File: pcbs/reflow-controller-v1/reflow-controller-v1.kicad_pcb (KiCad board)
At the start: 4 copper layers, 85.2 x 238.5 mm, 137 parts, among them J1 PinHeader 1x03 P2.54mm, J101 EB163A-03-C-180, J102 EB163A-02-C-180, J103 EB163A-02-C-180, J104 EB163A-02-C-180, J105 EB163A-02-C-180, J106 PinHeader 1x03 P2.54mm, J1101 EB163A-04-C-180, J1201 EB163A-04-C-180, J1301 EB163A-04-C-180, J2 PinHeader 1x02 P2.54mm, J3 SWD, J4 UART, M101 47053-1000, Q1 PMV65XP, SW1001 TS04-66-85-BK-160-SMT, SW1002 PEC12R-3220F-S0024, SW1003 TS04-66-85-BK-160-SMT, U1 TMP1075DSG, U1101 MAX31865ATP+, U1201 MAX31865ATP+, U1301 MAX31865ATP+, U2 TMP1075DSG, U201 TPS62933DRLR, U3 STM32G474VETx, U301 MOC3043SM, U401 MOC3043SM, U501 MOC3043SM, U601 MOC3043SM

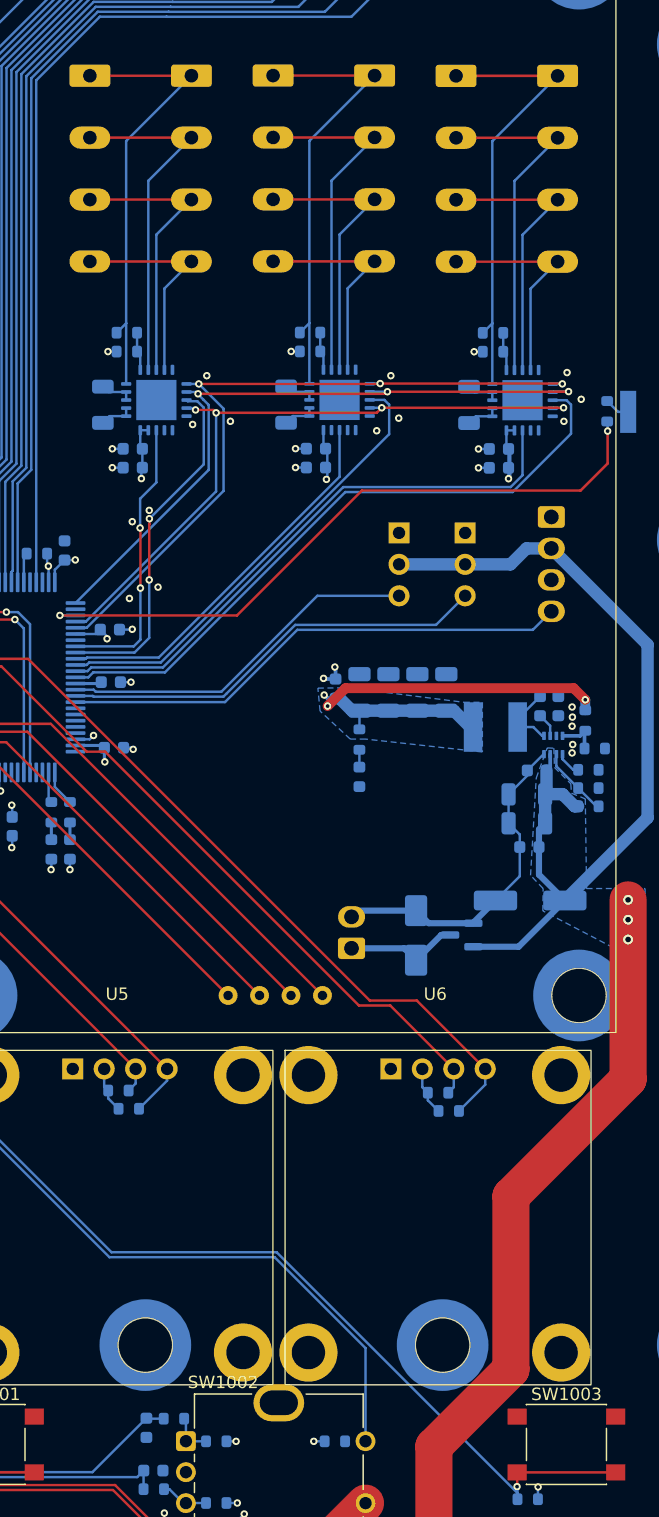
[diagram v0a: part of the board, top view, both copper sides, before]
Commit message: improve dfn qfn fanouts
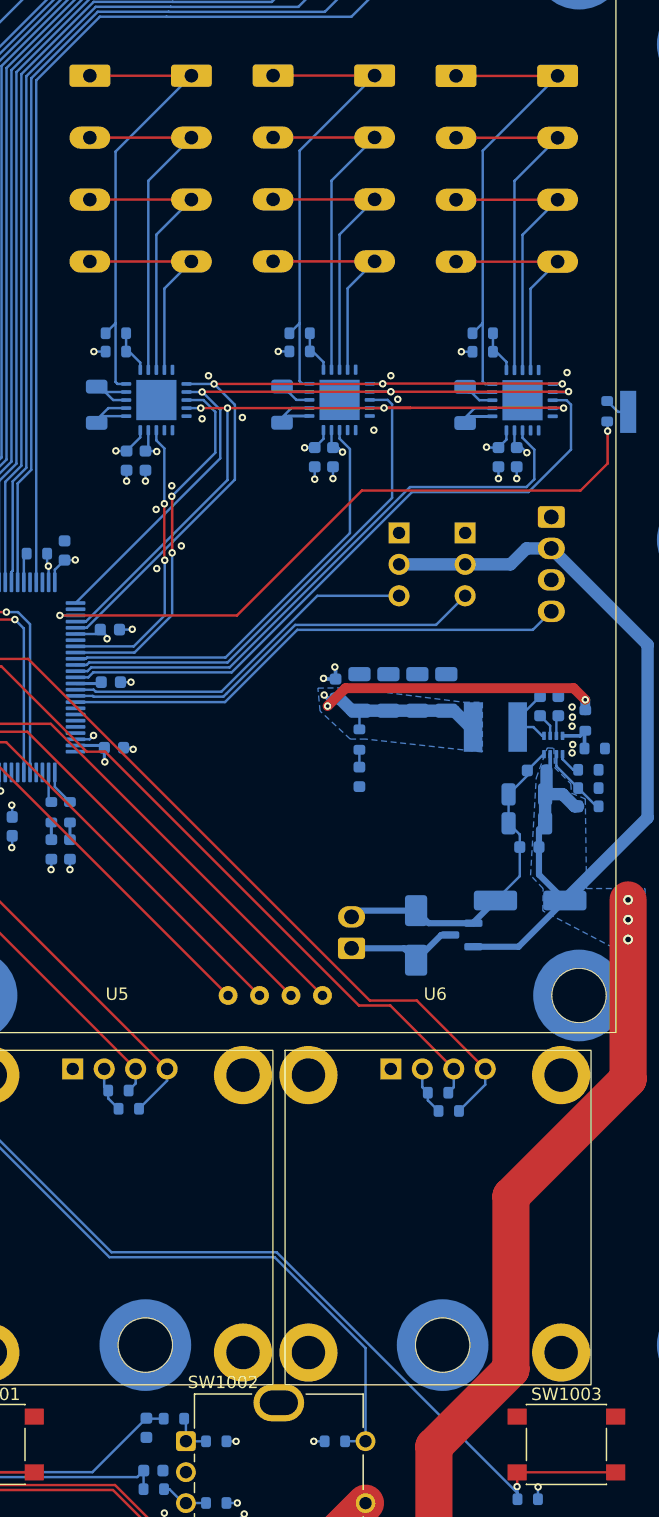
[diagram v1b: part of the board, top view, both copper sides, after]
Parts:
- moved C1302 1.67 mm to (82.5, 59.5), turned to -90 degrees
- moved C1202 1.61 mm to (67.7, 59.5), turned to -90 degrees
- moved C1101 1.17 mm to (52.6, 59.8), turned to -90 degrees
- moved C1102 1.08 mm to (51.1, 59.8), turned to -90 degrees
- moved R1103 0.89 mm to (50.2, 49.5)
- moved R1102 0.88 mm to (50.2, 51.0)
- moved R1203 0.84 mm to (65.0, 49.5)
- moved R1201 0.84 mm to (65.0, 51.0)
- moved R1303 0.83 mm to (79.8, 49.5)
- moved R1301 0.83 mm to (79.8, 51.0)
- moved C1201 0.70 mm to (66.2, 59.5), turned to -90 degrees
- moved C1301 0.66 mm to (81.1, 59.5), turned to -90 degrees
- moved R1101 0.50 mm to (48.6, 55.3)
- moved R1202 0.33 mm to (63.6, 55.3)
- moved R1302 0.32 mm to (78.4, 55.3)
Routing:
- net Net-(U1201-BIAS): track 2.76 -> 8.06 mm
- net Net-(U1301-BIAS): track 2.76 -> 8.05 mm
- net Net-(U1201-ISENSOR): track 2.71 -> 7.77 mm
- net Net-(U1301-ISENSOR): track 2.71 -> 7.76 mm
- net /Temperature sensor 2/~{DRDY}: track 31.2 -> 35.0 mm
- net /Temperature sensor 2/~{CS}: track 37.1 -> 40.7 mm
- net Net-(U1101-BIAS): track 2.76 -> 5.63 mm
- net /Temperature sensor 1/SDO: track 54.7 -> 57.5 mm
- net Net-(U1101-ISENSOR): track 2.71 -> 5.39 mm
- net /AC DC Converter/SS: track 0.00 -> 1.69 mm
- net /Buttons/SW_Encoder: track 79.5 -> 81.2 mm
- net /Temperature sensor 3/~{DRDY}: track 46.3 -> 47.8 mm
- net /Temperature sensor 1/SCLK: track 55.4 -> 56.6 mm
- net /Temperature sensor 1/FORCE+: track 36.4 -> 37.5 mm
- net /Temperature sensor 1/~{CS}: track 28.5 -> 29.6 mm
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
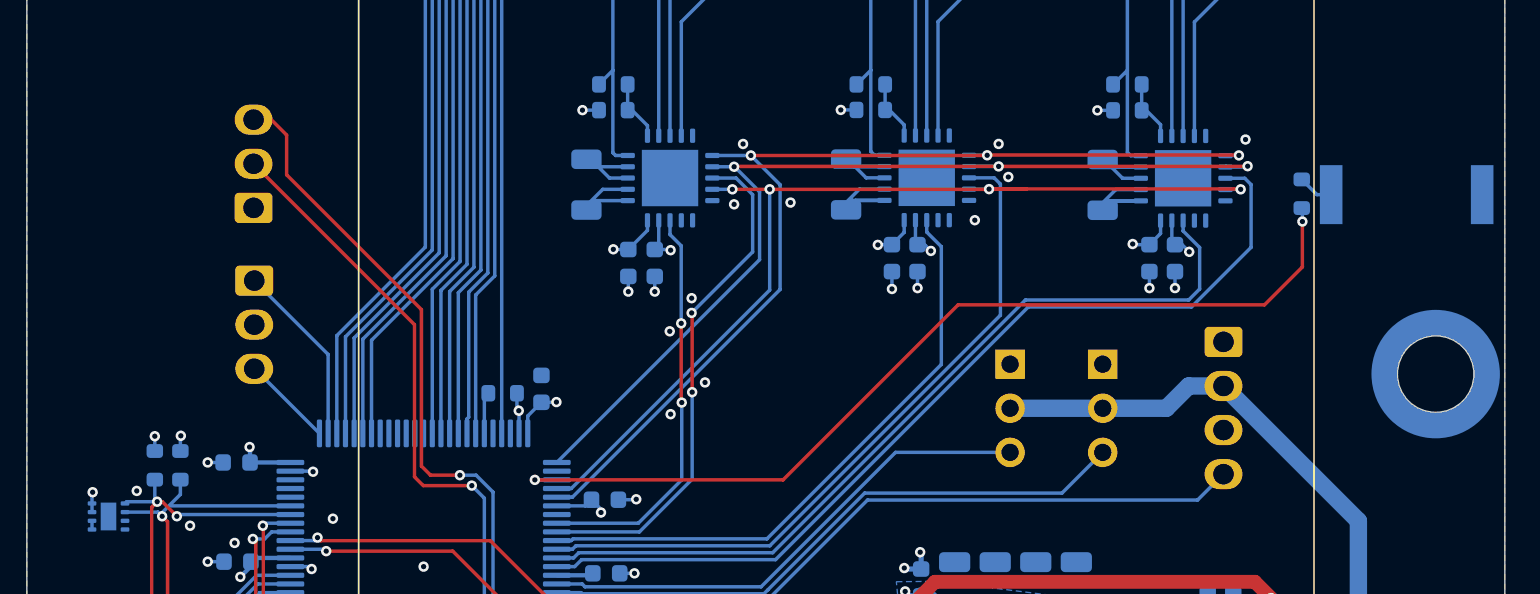
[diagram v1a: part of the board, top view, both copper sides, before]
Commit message: move beeper
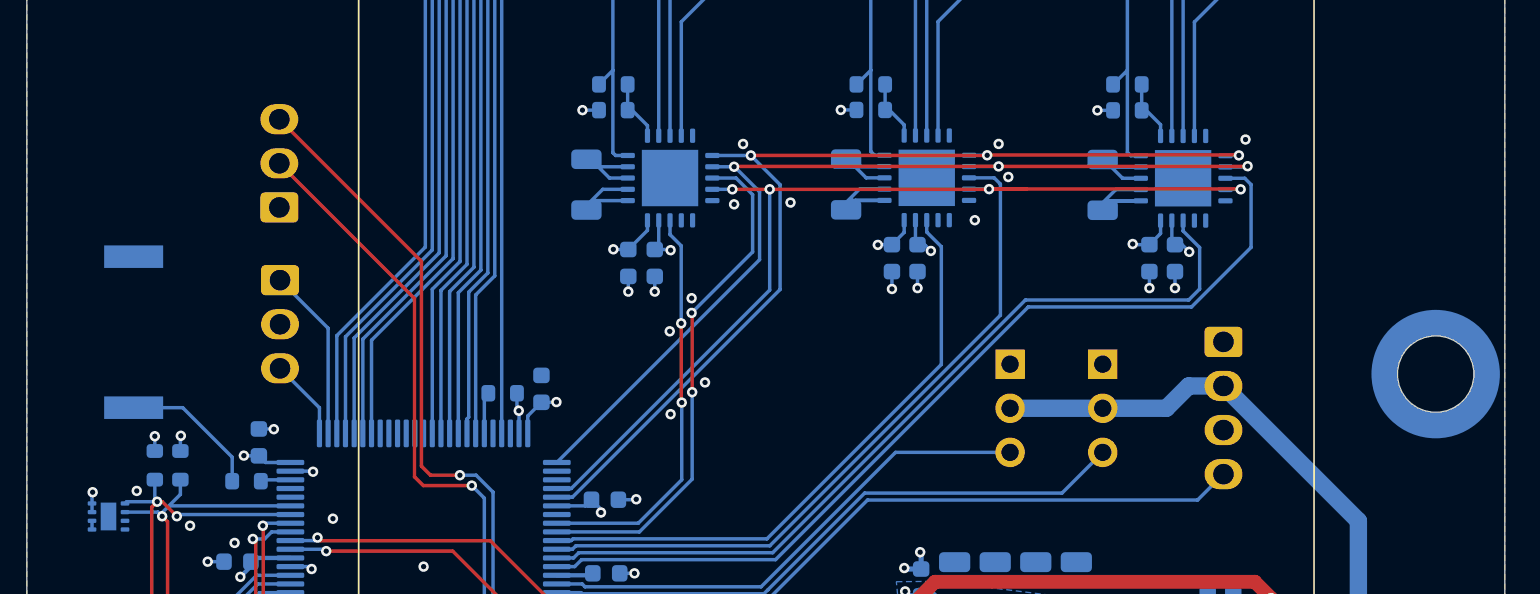
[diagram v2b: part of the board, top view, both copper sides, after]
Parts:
- moved BZ1 73.8 mm to (22.6, 63.8), turned to 90 degrees
- moved R5 63.0 mm to (29.1, 72.4), turned to 180 degrees
- moved C6 1.73 mm to (29.8, 70.2), turned to 90 degrees
- moved J4 1.48 mm to (30.9, 56.6)
- moved J3 1.48 mm to (31.0, 60.8)
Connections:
- U3 pad 3: /Buttons/Buzzer -> unconnected-(U3-PE4-Pad3)
- U3 pad 73: unconnected-(U3-PA12-Pad73) -> /Buttons/Buzzer
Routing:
- net /Buttons/Buzzer: track 54.0 -> 1.74 mm, vias 2 -> 0
- net Net-(BZ1-+): track 2.06 -> 8.24 mm
- net /microcontroller/USART1_TX: track 41.3 -> 40.1 mm
- net /microcontroller/SWDIO: track 5.30 -> 4.69 mm
- net /microcontroller/SWCLK: track 10.6 -> 9.98 mm
- net /microcontroller/USART1_RX: track 38.0 -> 37.4 mm

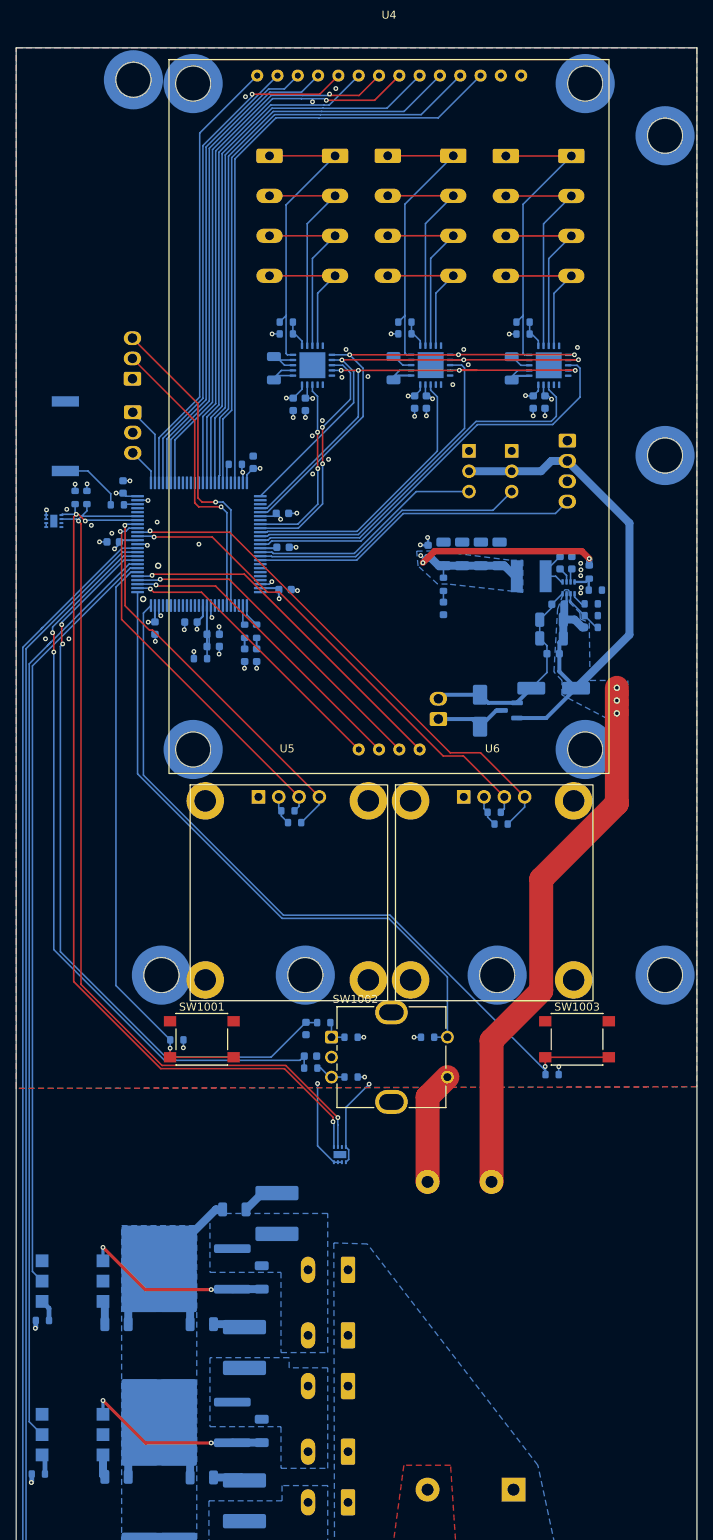
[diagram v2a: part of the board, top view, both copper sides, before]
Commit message: add zero crossing detector
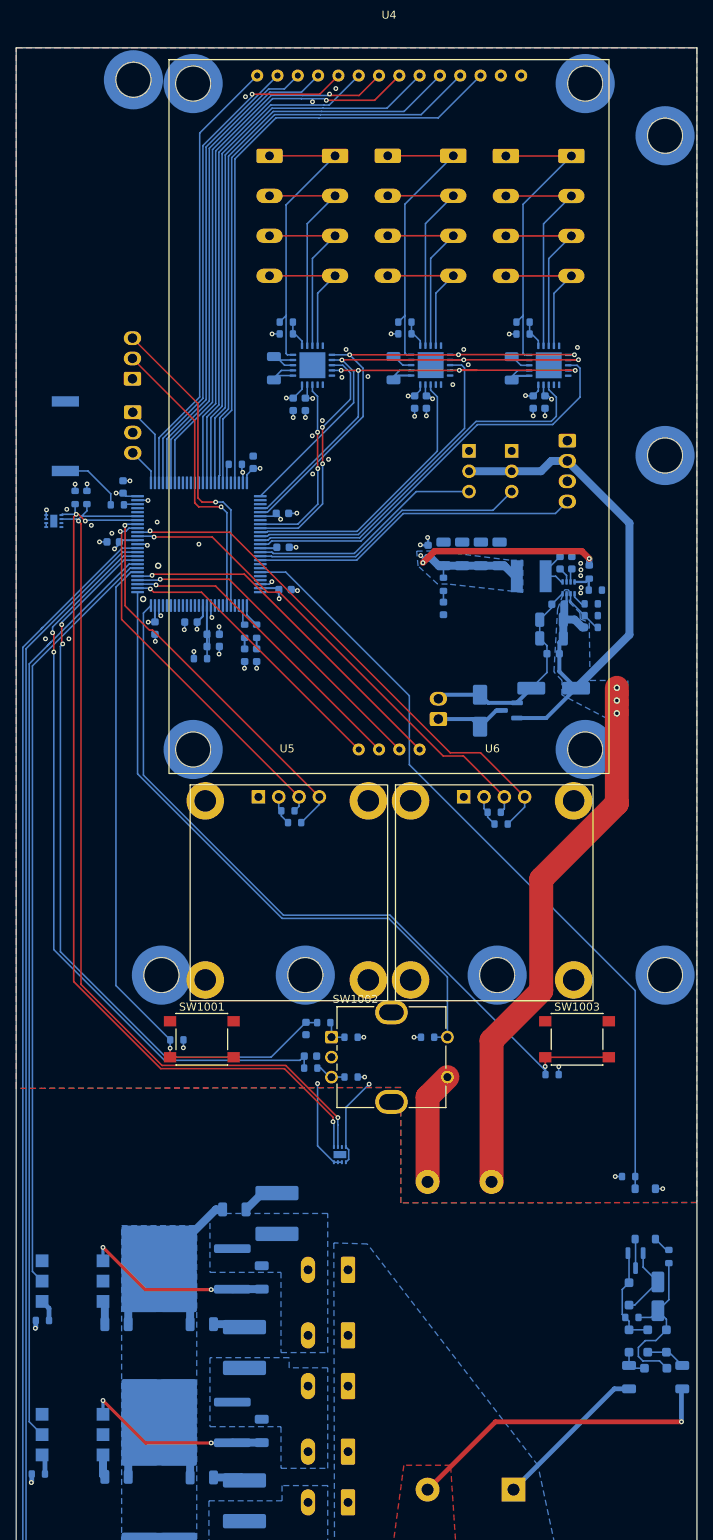
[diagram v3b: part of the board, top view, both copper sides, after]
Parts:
- added C1602: 10u, Capacitor_SMD:CP_Elec_4x5.7, B.Cu at (96.7, 171.4)
- added D1601: SL1K, Diode_SMD:D_SOD-123F, B.Cu at (97.7, 177.0)
- added D1602: SL1K, Diode_SMD:D_SOD-123F, B.Cu at (96.4, 180.4)
- added D1603: SL1K, Diode_SMD:D_SOD-123F, B.Cu at (93.1, 177.0)
- added D1604: SL1K, Diode_SMD:D_SOD-123F, B.Cu at (95.4, 177.0)
- added D1605: SL1K, Diode_SMD:D_SOD-123F, B.Cu at (93.1, 171.1)
- added Q1601: MMBT3904, Package_TO_SOT_SMD:SOT-23, B.Cu at (93.9, 166.9)
- added Q1602: 140357145200, wuerth:WL-OCPT_SOP4, B.Cu at (95.1, 161.1)
- added R1601: 220k, Resistor_SMD:R_1206_3216Metric, B.Cu at (99.7, 181.5)
- added R1602: 220k, Resistor_SMD:R_1206_3216Metric, B.Cu at (93.1, 181.5)
- added R1603: 1k, Resistor_SMD:R_0603_1608Metric, B.Cu at (98.0, 166.4)
- added R1604: 22k, Resistor_SMD:R_0603_1608Metric, B.Cu at (93.4, 174.0)
- added R1605: 10k, Resistor_SMD:R_0603_1608Metric, B.Cu at (93.0, 156.4)
- renumbered D1 to D202, Q1 to Q201
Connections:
- U3 pad 20: unconnected-(U3-PA0-Pad20) -> /Zero Crossing detector/Crossing
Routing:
- net /Zero Crossing detector/Crossing: track 0.00 -> 98.4 mm
- net /Phase_L: track 72.5 -> 111.9 mm, vias 15 -> 16
- net Net-(D1601-K): track 0.00 -> 21.9 mm
- net /Phase_N: track 0.00 -> 19.7 mm
- net Net-(D1603-A): track 0.00 -> 12.7 mm
- net Net-(D1605-A): track 0.00 -> 9.18 mm
- net Net-(D1601-A): track 0.00 -> 5.01 mm
- net Net-(D1602-A): track 0.00 -> 3.73 mm
- net Net-(Q1601-C): track 0.00 -> 3.65 mm
- net Net-(Q1602-Pad1): track 0.00 -> 2.24 mm
- net +3.3V: track 0.00 -> 0.91 mm, vias 0 -> 1
- net GND: track 81.5 -> 82.3 mm, vias 55 -> 56

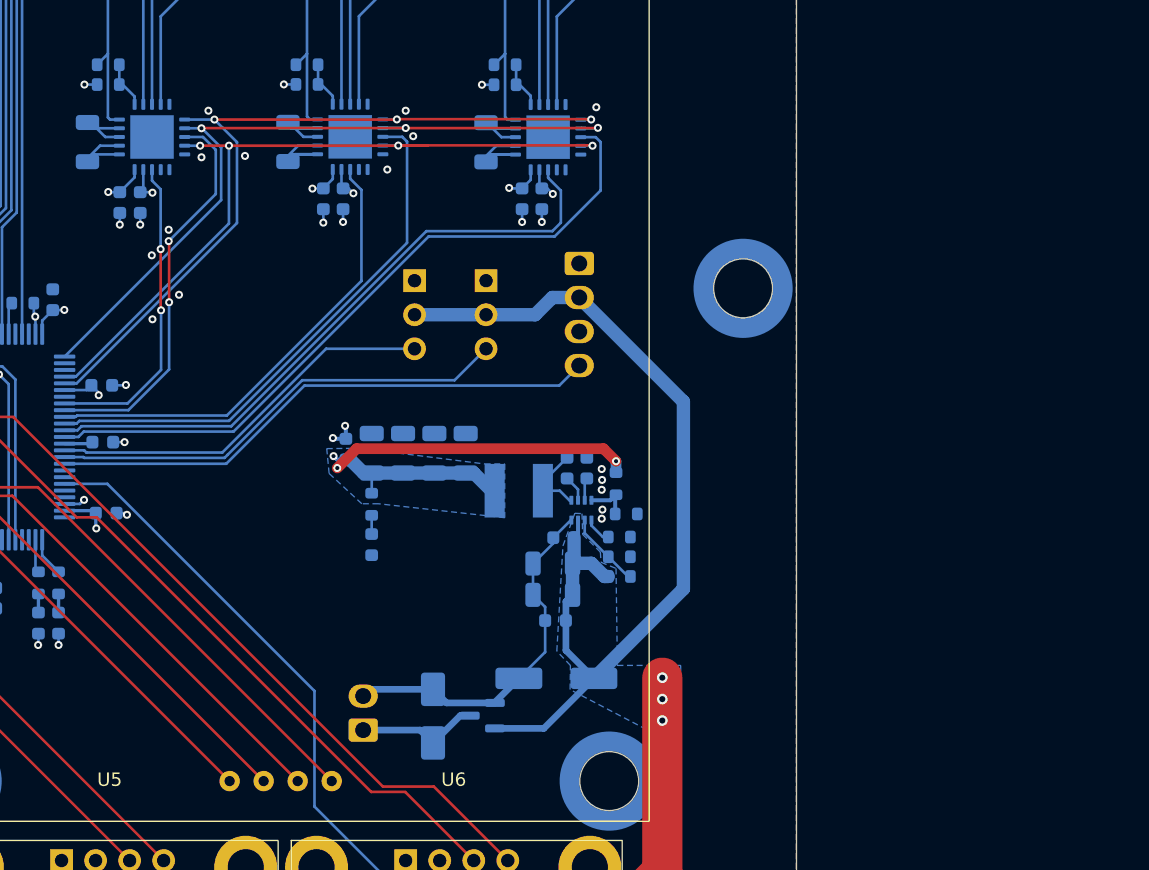
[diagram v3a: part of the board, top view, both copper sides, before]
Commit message: add ldo for analog voltage
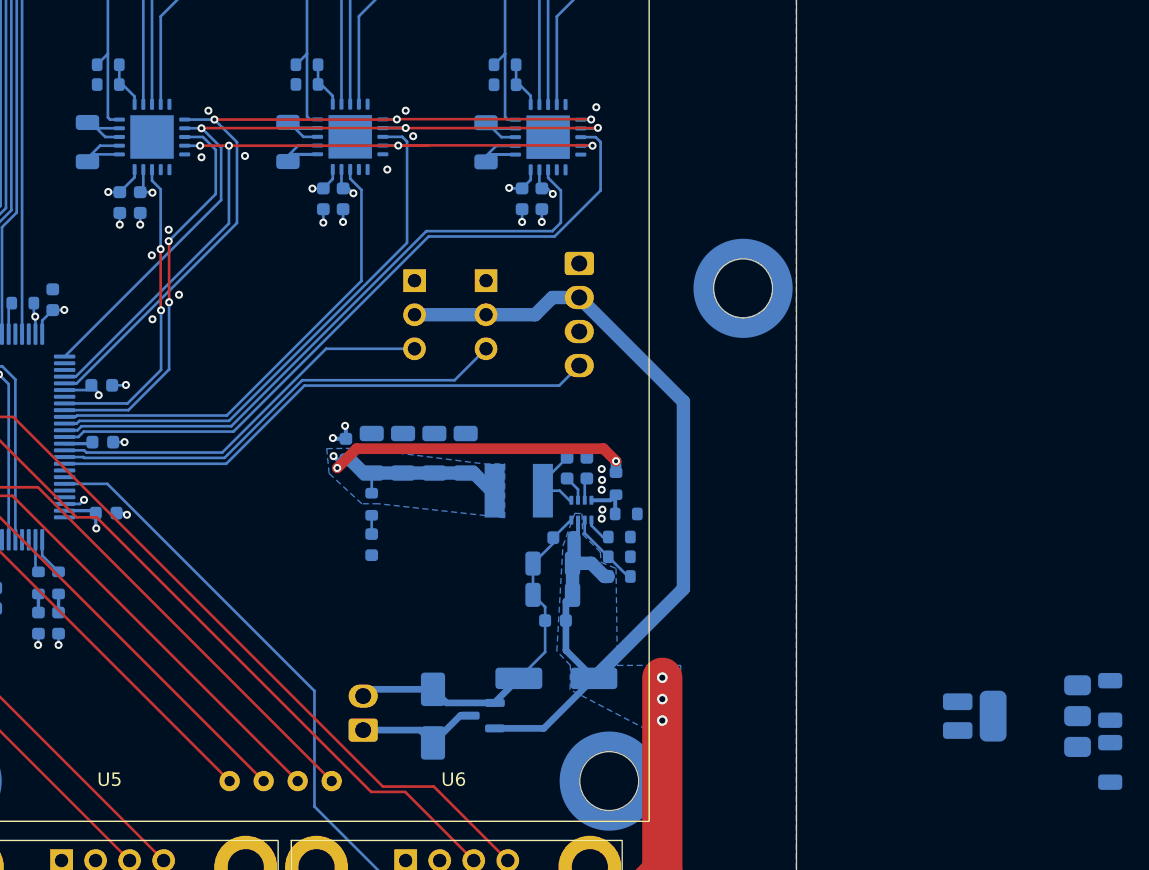
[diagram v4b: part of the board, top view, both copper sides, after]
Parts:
- added C213: 10u 35V, Capacitor_SMD:C_1206_3216Metric, B.Cu at (125.0, 101.6)
- added C214: 22u 10V, Capacitor_SMD:C_1206_3216Metric, B.Cu at (125.0, 97.0)
- added FB201: WE-RFI 744762439A, Inductor_SMD:L_1008_2520Metric, B.Cu at (113.6, 98.1)
- added U202: AZ1117-3.3, Package_TO_SOT_SMD:SOT-223-3_TabPin2, B.Cu at (119.4, 98.1)
- renumbered J2 to J201
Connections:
- C1101 pad 1: +3V3 -> +3.3VA
- C1202 pad 1: +3V3 -> +3.3VA
- C1302 pad 1: +3V3 -> +3.3VA
- Q1602 pad 4: +3.3V -> +3V3
- R1102 pad 2: GND -> GNDA
- R1201 pad 2: GND -> GNDA
- R1301 pad 2: GND -> GNDA
- U1101 pad 10: GND -> GNDA
- U1101 pad 16: GND -> GNDA
- U1101 pad 20: +3V3 -> +3.3VA
- U1101 pad 21: GND -> GNDA
- U1201 pad 10: GND -> GNDA
- U1201 pad 16: GND -> GNDA
- U1201 pad 20: +3V3 -> +3.3VA
- U1201 pad 21: GND -> GNDA
- U1301 pad 10: GND -> GNDA
- U1301 pad 16: GND -> GNDA
- U1301 pad 20: +3V3 -> +3.3VA
- U1301 pad 21: GND -> GNDA
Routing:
- net GND: track 82.3 -> 79.5 mm, vias 56 -> 53
- net +3V3: track 109.3 -> 110.2 mm, vias 32 -> 33
- net +3.3V: track 0.91 -> 0.00 mm, vias 1 -> 0
